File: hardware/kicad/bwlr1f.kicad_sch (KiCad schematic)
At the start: 59 parts, among them J1 Conn_01x02, Q2 PMV32UP, U1 BME688, U1 NBM7100ABQX, U2 RAK3172-SIP, U3 ZD24C16A, U4 TPL5110DDCT

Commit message: add notes
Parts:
- C10: DPN (none) -> C1525; Distributor (none) -> LCSC; MPN (none) -> CL05B104KO5NNNC; Manufacturer YAGEO -> Samsung Electro-Mechanics
- C16: renamed from C13; DPN (none) -> 581-TCJ5477M016R100E; Distributor (none) -> Mouser; MPN (none) -> TCJ5477M016R0100E; Manufacturer (none) -> KYOCERA AVX
- C3: DPN (none) -> C1525; Distributor (none) -> LCSC; MPN (none) -> CL05B104KO5NNNC; Manufacturer (none) -> Samsung Electro-Mechanics
- C3: DPN (none) -> C29266; Distributor (none) -> LCSC; MPN (none) -> CL05A105KO5NNNC; Manufacturer (none) -> Samsung Electro-Mechanics
- C3: DPN (none) -> C7472972; Distributor (none) -> LCSC; MPN (none) -> HGC1206R7226K160NSPJ; Manufacturer (none) -> Chinocera
- C3, C5: value 100n -> 100nF; DPN (none) -> C1525; Distributor (none) -> LCSC; MPN (none) -> CL05B104KO5NNNC; Manufacturer (none) -> Samsung Electro-Mechanics
- C3: DPN (none) -> C47339; Distributor (none) -> LCSC; MPN (none) -> CL05A474KP5NNNC; Manufacturer (none) -> Samsung Electro-Mechanics
- C3: footprint Capacitor_SMD:C_0402_1005Metric -> Capacitor_SMD:C_0603_1608Metric; DPN (none) -> C962136; Distributor (none) -> LCSC; MPN (none) -> CL10A106KO8NQNC; Manufacturer (none) -> Samsung Electro-Mechanics
- C3: DPN (none) -> C368809; Distributor (none) -> LCSC; MPN (none) -> CL05A475KP5NRNC; Manufacturer (none) -> Samsung Electro-Mechanics
- E1: DPN (none) -> 712-ANT-915-USP410; Distributor (none) -> Mouser; MPN (none) -> ANT-915-uSP410
- L1: DPN (none) -> C709642; Distributor (none) -> LCSC; MPN (none) -> MZAS1608G121-1R3TF; Manufacturer (none) -> Sunlord
- L2: footprint Inductor_SMD:L_1206_3216Metric -> Inductor_SMD:L_0805_2012Metric; DPN (none) -> C383402; Distributor (none) -> LCSC; MPN (none) -> MLZ2012M150WT000; Manufacturer (none) -> TDK
- L2: DPN (none) -> 710-74404042150; Distributor (none) -> Mouser; MPN (none) -> 74404042150; Manufacturer (none) -> Wurth Elektronik
- L3: renamed from L4; DPN (none) -> C709642; Distributor (none) -> LCSC; MPN (none) -> MZAS1608G121-1R3TF; Manufacturer (none) -> Sunlord
- L4: renamed from L5; DPN (none) -> C709642; Distributor (none) -> LCSC; MPN (none) -> MZAS1608G121-1R3TF; Manufacturer (none) -> Sunlord
- Q2: DPN (none) -> C2959851; Distributor (none) -> LCSC; LCSC C2959851 -> (none); MPN (none) -> PMV32UP; Manufacturer (none) -> TECH PUBLIC
- R10: DPN (none) -> C163488; Distributor (none) -> LCSC; MPN (none) -> RC0402FR-0716K9L
- R11: DPN (none) -> C60491; Distributor (none) -> LCSC; MPN (none) -> RC0402FR-07100KL; Manufacturer (none) -> YAGEO
- R11: DPN (none) -> C138033; Distributor (none) -> LCSC; MPN (none) -> RC0402FR-071ML
- R2, R3: DPN (none) -> C60490; Distributor (none) -> LCSC; MPN (none) -> RC0402FR-0710KL; Manufacturer (none) -> YAGEO
- R4: DPN (none) -> C106235; Distributor (none) -> LCSC; MPN (none) -> RC0402FR-071KL; Manufacturer (none) -> YAGEO
- R4, R5: DPN (none) -> C105871; Distributor (none) -> LCSC; MPN (none) -> RC0402FR-074K7L
- R5: DPN (none) -> C60490; Distributor (none) -> LCSC; MPN (none) -> RC0402FR-0710KL
- U1: renamed from U2; DPN (none) -> 306039; Distributor (none) -> RAKwireless; MPN (none) -> RAK3172-SIP; Manufacturer (none) -> RAKwireless
- U1: DPN (none) -> C3664478; Distributor (none) -> LCSC; MPN (none) -> BME688
- U2: renamed from U1; DPN (none) -> 771-NBM7100ABQX; Distributor (none) -> Mouser; MPN (none) -> NBM7100ABQX; Manufacturer (none) -> Nexperia
- U3: value ZD24C16A -> ZD24C08A; DPN (none) -> C2896640; Distributor (none) -> LCSC; MPN (none) -> ZD24C08A-STGMT; Manufacturer (none) -> Zetta
- U4: DPN (none) -> C125830; Distributor (none) -> LCSC; MPN (none) -> TPL5110DDCT
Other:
- note added: "+/- 30s"
- note added: "ANTENNA"
- note added: "Coplanar Waveguide With Ground Characteristic"
- note added: "Effective Dielectric Constant: 2.33 Characteristic Impedance: 50.19ohm"
- note added: "Power Gating Time Interval:"
- note added: "RAK3172-SIP"
- note added: "Relative Dielectric Constant: 4.5 Track Width : 0.8mm Gap Width : 0.15mm Dielectric Thickness : 1.6mm"
- note added: "Trace characteristics"
- note removed: "6.3V ceramic"
- note removed: "Antenna"
- note removed: "MCU"
- moved on the sheet: C10, C15, C16, C3, C5, E1, J1, L1, L2, L3, L4, Q2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

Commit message: finish bom & cpl
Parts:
- C10: DPN C1525 -> (none); Distributor LCSC -> (none); MPN CL05B104KO5NNNC -> (none); Manufacturer Part Number (none) -> CL05B104KO5NNNC; Part Number CC0603KRX7R7BB104 -> (none)
- C16: DPN 581-TCJ5477M016R100E -> (none); Distributor Mouser -> (none); MPN TCJ5477M016R0100E -> (none); Manufacturer Part Number (none) -> TCJ5477M016R0100E
- C3, C5: DPN C1525 -> (none); Distributor LCSC -> (none); MPN CL05B104KO5NNNC -> (none); Manufacturer Part Number (none) -> CL05B104KO5NNNC
- C3: DPN C29266 -> (none); Distributor LCSC -> (none); MPN CL05A105KO5NNNC -> (none); Manufacturer Part Number (none) -> CL05A105KO5NNNC
- C3: DPN C7472972 -> (none); Distributor LCSC -> (none); MPN HGC1206R7226K160NSPJ -> (none); Manufacturer Part Number (none) -> HGC1206R7226K160NSPJ
- C3: DPN C47339 -> (none); Distributor LCSC -> (none); MPN CL05A474KP5NNNC -> (none); Manufacturer Part Number (none) -> CL05A474KP5NNNC
- C3: DPN C962136 -> (none); Distributor LCSC -> (none); MPN CL10A106KO8NQNC -> (none); Manufacturer Part Number (none) -> CL10A106KO8NQNC
- C3: DPN C368809 -> (none); Distributor LCSC -> (none); MPN CL05A475KP5NRNC -> (none); Manufacturer Part Number (none) -> CL05A475KP5NRNC
- E1: DPN 712-ANT-915-USP410 -> (none); Distributor Mouser -> (none); MPN ANT-915-uSP410 -> (none); Manufacturer Part Number (none) -> ANT-915-uSP410; Part Number ANT-915-USP410 -> (none)
- L1, L3, L4: DPN C709642 -> (none); Distributor LCSC -> (none); MPN MZAS1608G121-1R3TF -> (none); Manufacturer Part Number (none) -> MZAS1608G121-1R3TF
- L2: DPN C383402 -> (none); Distributor LCSC -> (none); MPN MLZ2012M150WT000 -> (none); Manufacturer Part Number (none) -> MLZ2012M150WT000
- L2: DPN 710-74404042150 -> (none); Distributor Mouser -> (none); MPN 74404042150 -> (none); Manufacturer Part Number (none) -> 74404042150
- Q2: DPN C2959851 -> (none); Distributor LCSC -> (none); MPN PMV32UP -> (none); Manufacturer Part Number (none) -> PMV32UP
- R10: DPN C163488 -> (none); Distributor LCSC -> (none); MPN RC0402FR-0716K9L -> (none); Manufacturer Part Number (none) -> RC0402FR-0716K9L; Part Number AC0603FR-0716K9L -> (none)
- R11: DPN C60491 -> (none); Distributor LCSC -> (none); MPN RC0402FR-07100KL -> (none); Manufacturer Part Number (none) -> RC0402FR-07100KL
- R11: DPN C138033 -> (none); Distributor LCSC -> (none); MPN RC0402FR-071ML -> (none); Manufacturer Part Number (none) -> RC0402FR-071ML; Part Number RC0603DR-071ML -> (none)
- R2, R3: DPN C60490 -> (none); Distributor LCSC -> (none); MPN RC0402FR-0710KL -> (none); Manufacturer Part Number (none) -> RC0402FR-0710KL
- R4: DPN C106235 -> (none); Distributor LCSC -> (none); MPN RC0402FR-071KL -> (none); Manufacturer Part Number (none) -> RC0402FR-071KL
- R4, R5: DPN C105871 -> (none); Distributor LCSC -> (none); MPN RC0402FR-074K7L -> (none); Manufacturer Part Number (none) -> RC0402FR-074K7L; Part Number RC0603FR-0710KL -> (none)
- R5: DPN C60490 -> (none); Distributor LCSC -> (none); MPN RC0402FR-0710KL -> (none); Manufacturer Part Number (none) -> RC0402FR-0710KL; Part Number RC0603FR-0710KL -> (none)
- U1: DPN 306039 -> (none); Distributor RAKwireless -> (none); MPN RAK3172-SIP -> (none); Manufacturer Part Number (none) -> RAK3172-SIP
- U1: DPN C3664478 -> (none); Distributor LCSC -> (none); MPN BME688 -> (none); Manufacturer Part Number (none) -> BME688; Part Number BME688 -> (none)
- U2: DPN 771-NBM7100ABQX -> (none); Distributor Mouser -> (none); MPN NBM7100ABQX -> (none); Manufacturer Part Number (none) -> NBM7100ABQX
- U3: DPN C2896640 -> (none); Distributor LCSC -> (none); MPN ZD24C08A-STGMT -> (none); Manufacturer Part Number (none) -> ZD24C08A-STGMT
- U4: DPN C125830 -> (none); Distributor LCSC -> (none); MPN TPL5110DDCT -> (none); Manufacturer Part Number (none) -> TPL5110DDCT; Part Number TPL5110DDCT -> (none)

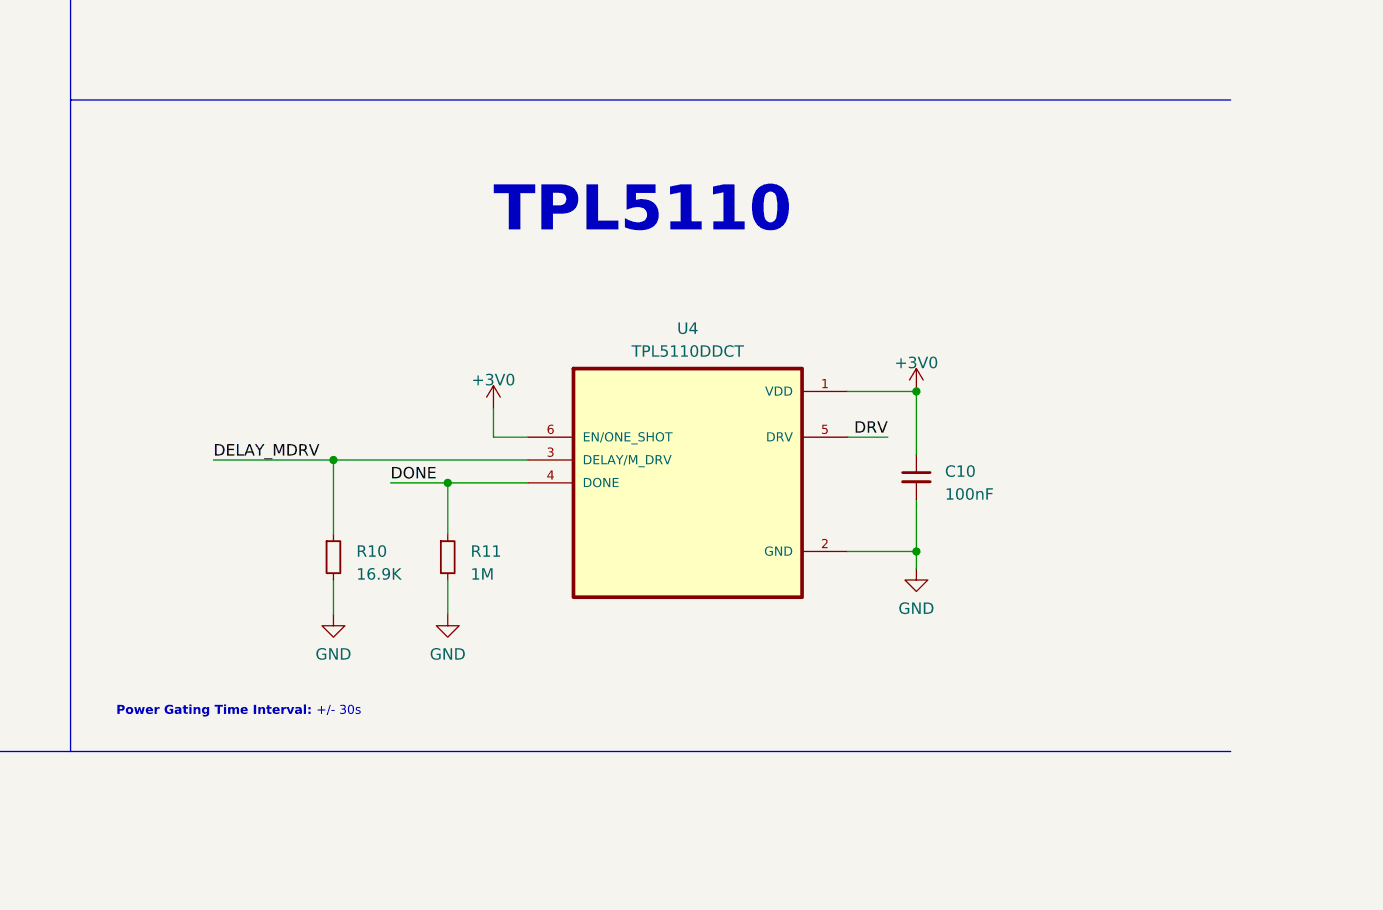
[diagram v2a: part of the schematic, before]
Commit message: add mosfet switch for M_DRV
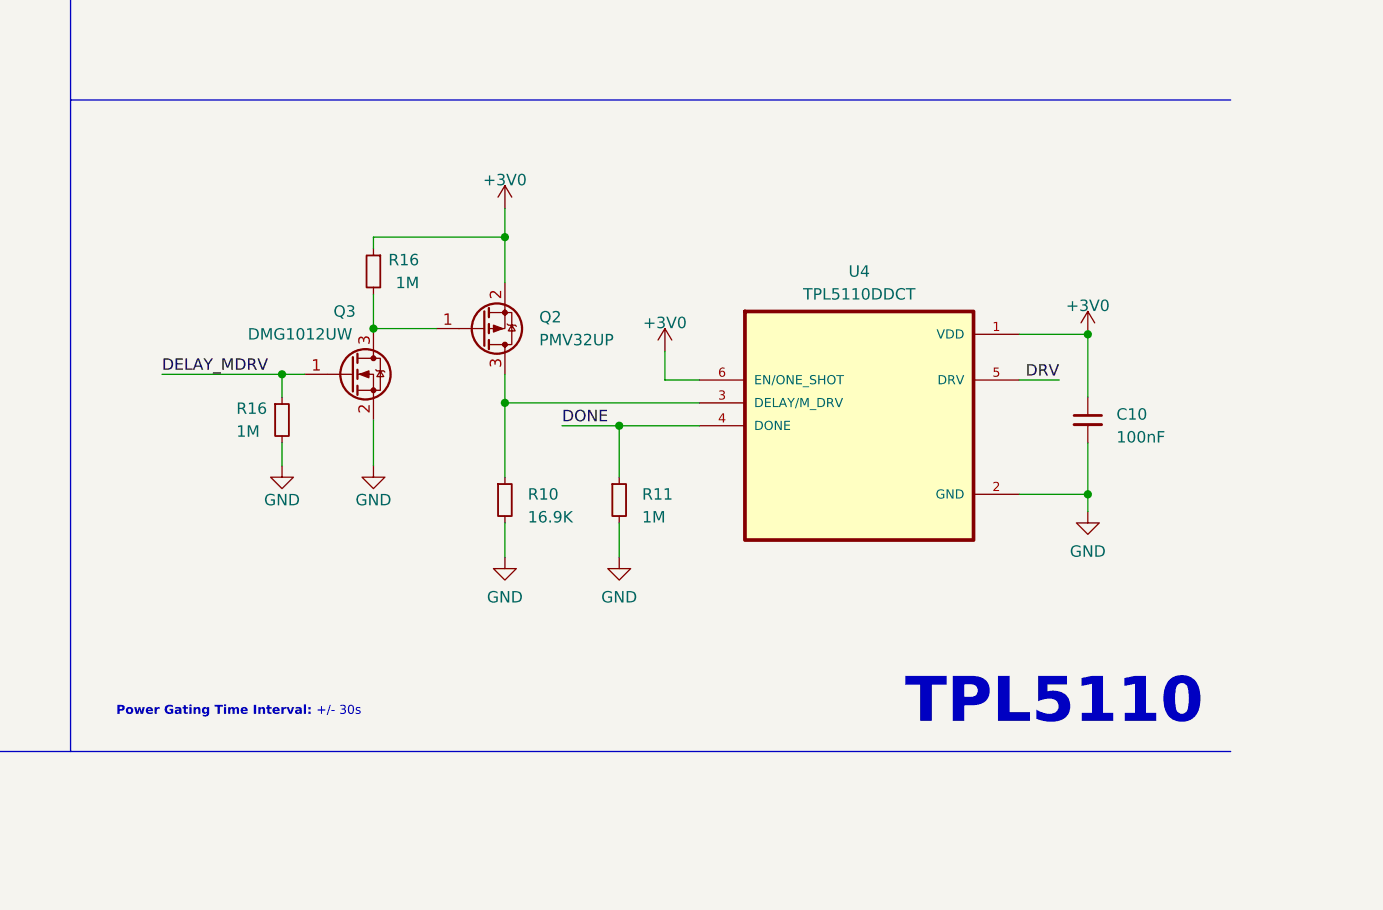
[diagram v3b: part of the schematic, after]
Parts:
- added Q2: PMV32UP, Package_TO_SOT_SMD:SOT-23, symbol Device:Q_PMOS_GSD
- added Q3: DMG1012UW, Package_TO_SOT_SMD:SOT-323_SC-70, symbol Device:Q_NMOS_GSD
- added R16 (x2): 1M, Resistor_SMD:R_0402_1005Metric, symbol Device:R_Small
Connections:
- net +3V0: now also Q2.2 (S), R16.1
- net DELAY_MDRV: now also Q3.1 (G), R16.1; no longer R10.1, U4.3 (DELAY/M_DRV)
- net GND: now also Q3.2 (S), R16.2
- new net: Q2.3 (D), R10.1, U4.3 (DELAY/M_DRV)
- new net: Q2.1 (G), Q3.3 (D), R16.2
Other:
- moved on the sheet: C10, R10, R11, U4

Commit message: wip: re-layout
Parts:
- added C3: 1uF, Capacitor_SMD:C_0402_1005Metric, symbol Device:C_Small
- added JP1: OUTPUT_SELECT, Jumper:SolderJumper-3_P1.3mm_Open_RoundedPad1.0x1.5mm, symbol Jumper:SolderJumper_3_Open
- C3: Part Description (none) -> 16V, X7R, <10%
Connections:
- net +3V0: now also C3.2; no longer C10.1, C3.2, Q2.2 (S), R16.1, U4.1 (VDD), U4.6 (EN/ONE_SHOT)
- net BATT+: now also C10.1, Q2.2 (S), R16.1, U4.1 (VDD), U4.6 (EN/ONE_SHOT)
- net GND: now also C3.1
- net RDY: now also U1.18 (PB7/UART1_RX); no longer U1.19 (PB8)
- net START: now also U1.17 (PB6/UART1_TX); no longer U1.20 (PB9)
- net +VDP: now reaches C3.1, R4.1, R4.1, U2.15 (VDP)
- net +VDP: now also JP1.1 (A)
- net at U2.14 (VDH), U2.9 (VDHS): now also C3.2, JP1.3 (B); no longer Q2.3 (S)
- new net: JP1.2 (C), Q2.3 (S)
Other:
- note removed: "16V, X7R, <10%"
- moved on the sheet: C3, Q2

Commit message: wip: initial pcb prod
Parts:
- removed E1: ANT-915-USP410, Teapot:XDCR_ANT-915-USP410, symbol bwlr1e:ANT-915-USP410
- removed U4: TPL5110DDCT, Teapot:SOT95P280X110-6N, symbol cwlr1a:TPL5110DDCR
- added E1: ANT-915-USP410, bwlr1f:XDCR_ANT-915-USP410, symbol bwlr1f:ANT-915-USP410
- added U5: TPL5110, Package_TO_SOT_SMD:SOT-23-6, symbol Timer:TPL5110
- C16: footprint Teapot:CAPPM7362X200N -> Capacitor_Tantalum_SMD:CP_EIA-7343-40_Kemet-Y
- J1: footprint Teapot:Battery_Pad -> bwlr1f:Battery_Pad
- L2: footprint Teapot:74404042150 -> bwlr1f:74404042150
- U1: footprint Teapot:RAK3172-SiP_LGA75 -> bwlr1f:RAK3172-SiP_LGA75; Manufacturer RAKwireless -> (none); Manufacturer Part Number RAK3172-SIP -> (none)
- U1: footprint Teapot:BME680-PSON80P300X300X100-8N -> bwlr1f:BME680-PSON80P300X300X100-8N
- U2: footprint Teapot:NBM7100ABQX -> bwlr1f:NBM7100ABQX
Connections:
- net ANT: now also E1.1
- net BATT+: now also U5.1 (VDD), U5.6 (EN/ONE_SHOT)
- net DONE: now also U5.4 (DONE)
- net DRV: now also U5.5 (DRV)
- net GND: now also E1.2, U5.2 (GND)
- net at Q2.3 (D), R10.1: now also U5.3 (DELAY/M_DRV)
- no-connect marks 24 -> 27
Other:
- moved on the sheet: C10, R11

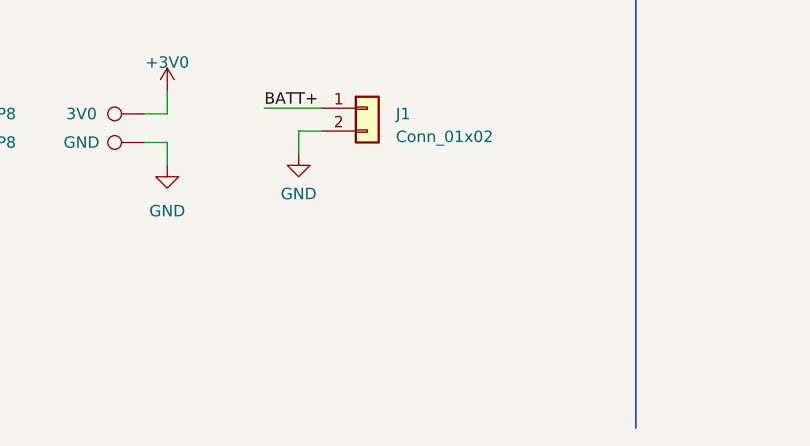
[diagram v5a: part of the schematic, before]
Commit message: add battery pack
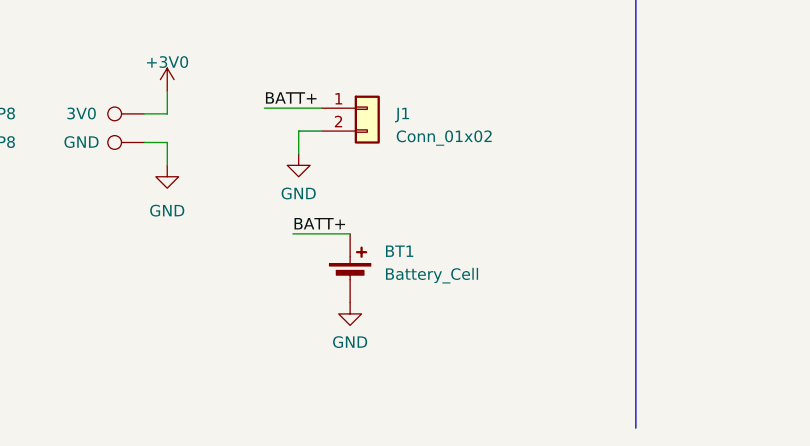
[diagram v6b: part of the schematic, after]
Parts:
- added BT1: Battery_Cell, bwlr1f:BAT-SMD_MY-2032-12, symbol Device:Battery_Cell
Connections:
- net BATT+: now also BT1.1 (+)
- net GND: now also BT1.2 (-)
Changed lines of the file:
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@@
     (stroke (width 0) (type default))
   )
+  (wire (pts (xy 72.39 263.525) (xy 78.74 263.525))
+    (stroke (width 0) (type default))
+  )
   (wire (pts (xy 127 59.055) (xy 129.54 59.055))
     (stroke (width 0) (type default))
@@
     (effects (font (size 1.27 1.27)) (justify left bottom))
   )
+  (label "BATT+" (at 72.39 263.525 0) (fields_autoplaced)
+    (effects (font (size 1.27 1.27)) (justify left bottom))
+  )
   (label "RDY" (at 101.6 165.1 90) (fields_autoplaced)
     (effects (font (size 1.27 1.27)) (justify left bottom))
@@
     )
   )
+  (symbol (lib_id "power:GND") (at 78.74 271.145 0) (unit 1)
+    (in_bom yes) (on_board yes) (dnp no)
+    (property "Reference" "#PWR023" (at 78.74 277.495 0)
+      (effects (font (size 1.27 1.27)) hide)
+    )
+    (property "Value" "GND" (at 78.74 275.59 0)
+      (effects (font (size 1.27 1.27)))
+    )
+    (property "Footprint" "" (at 78.74 271.145 0)
+      (effects (font (size 1.27 1.27)) hide)
+    )
+    (property "Datasheet" "" (at 78.74 271.145 0)
+      (effects (font (size 1.27 1.27)) hide)
+    )
+    (pin "1")
+    (instances
+      (project "cwlr1a"
+        (path "/7b840fb1-9a2f-4853-9d9a-85bf1e1432ed"
+          (reference "#PWR023") (unit 1)
+        )
+      )
+      (project "bwlr1f"
+        (path "/7fec048a-2dfd-4bff-8685-e805b00dfe07"
+          (reference "#PWR052") (unit 1)
+        )
+      )
+    )
+  )
   (symbol (lib_id "Device:R_Small") (at 363.22 62.865 270) (mirror x) (unit 1)
     (in_bom yes) (on_board yes) (dnp no)
@@
         )
       )
+    )
+  )
+  (symbol (lib_id "Device:Battery_Cell") (at 78.74 268.605 0) (unit 1)
+    (in_bom yes) (on_board yes) (dnp no) (fields_autoplaced)
+    (property "Reference" "BT1" (at 82.55 265.4935 0)
+      (effects (font (size 1.27 1.27)) (justify left))
+    )
+    (property "Value" "Battery_Cell" (at 82.55 268.0335 0)
+      (effects (font (size 1.27 1.27)) (justify left))
+    )
+    (property "Footprint" "bwlr1f:BAT-SMD_MY-2032-12" (at 78.74 267.081 90)
+      (effects (font (size 1.27 1.27)) hide)
+    )
+    (property "Datasheet" "~" (at 78.74 267.081 90)
+      (effects (font (size 1.27 1.27)) hide)
+    )
+    (property "Part Description" "" (at 78.74 268.605 0)
+      (effects (font (size 1.27 1.27)) hide)
+    )
+    (property "Manufacturer" "" (at 78.74 268.605 0)
+      (effects (font (size 1.27 1.27)) hide)
+    )
+    (property "Manufacturer Part Number" "" (at 78.74 268.605 0)
+      (effects (font (size 1.27 1.27)) hide)
+    )
+    (property "Distributor" "" (at 78.74 268.605 0)
+      (effects (font (size 1.27 1.27)) hide)
+    )
+    (property "Distributor Part Number" "" (at 78.74 268.605 0)
+      (effects (font (size 1.27 1.27)) hide)
+    )
+    (property "Distributor Link" "" (at 78.74 268.605 0)
+      (effects (font (size 1.27 1.27)) hide)
+    )
+    (pin "1")
+    (pin "2")
+    (instances
+      (project "bwlr1f"
+        (path "/7fec048a-2dfd-4bff-8685-e805b00dfe07"
+          (reference "BT1") (unit 1)
+        )
+      )
